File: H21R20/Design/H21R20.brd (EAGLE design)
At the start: 34.6 x 30 mm, 52 parts, among them IC1 ESP32-C3-MINI-1-N4, P1 HEXABIT_17.32_NO_P6_P7_P12, U1 STM32G0B1CEU6NUFQFPN48_STM32_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, X1 8MHZ

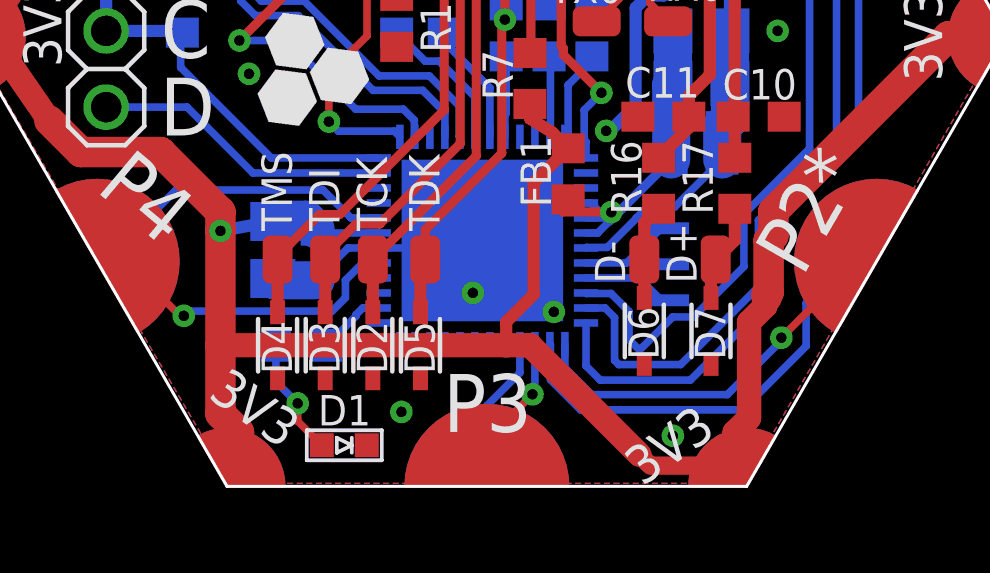
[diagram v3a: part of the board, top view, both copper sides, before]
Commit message: -Correcting some documentaion issues
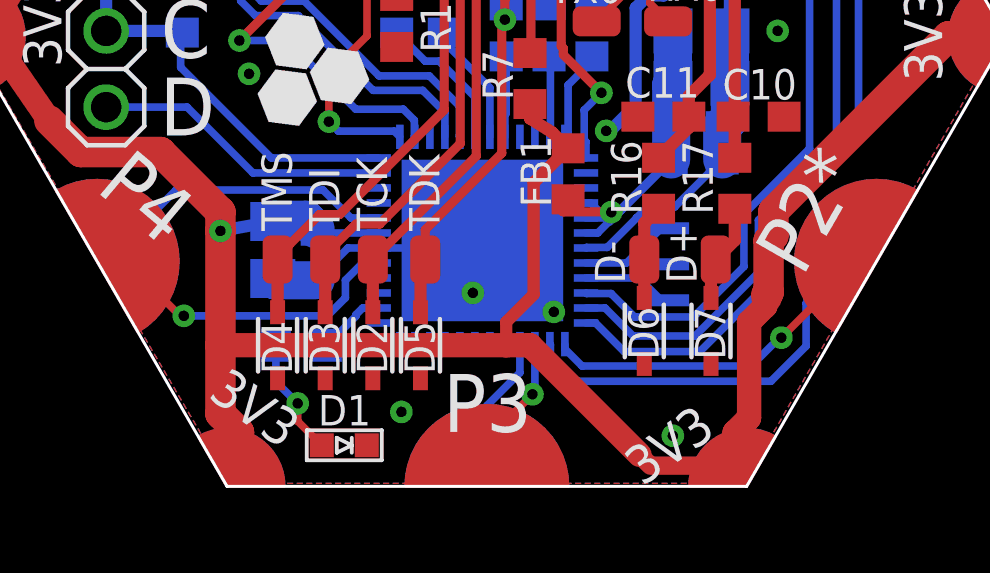
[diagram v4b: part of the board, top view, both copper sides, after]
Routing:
- net USART4_RX: track 26.0 -> 24.0 mm
- net USART4_TX: track 25.3 -> 23.4 mm
- net N$12: track 21.0 -> 19.6 mm
- net USART2_TX: track 13.5 -> 12.3 mm
- net USART2_RX: track 14.9 -> 13.8 mm
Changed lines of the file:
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@@
 <?xml version="1.0" encoding="utf-8"?>
 <!DOCTYPE eagle SYSTEM "eagle.dtd">
-<eagle version="9.6.2">
+<eagle version="9.6.1">
 <drawing>
 <settings>
-<setting alwaysvectorfont="no"/>
+<setting alwaysvectorfont="yes"/>
 <setting verticaltext="up"/>
 </settings>
@@
 </layers>
 <board>
-<fusionsync huburn="a.YnVzaW5lc3M6Z21haWwyMzYzMzA4" projecturn="a.YnVzaW5lc3M6Z21haWwyMzYzMzA4I0QyMDIyMDIyNzUwMTk3Njc4MQ" f3durn="urn:adsk.wipprod:dm.lineage:qXE8OnRfQE6j2yabujY-pQ" pcbguid="" lastpulledtime="" lastsyncedchangeguid="" latestrevisionid="54fbac2f-ec53-449b-82c3-dd918a9148f3" lastsyncedrevisionid="54fbac2f-ec53-449b-82c3-dd918a9148f3" lastboardhashguid="b3c6bdbd-b9b3-ff31-31e0-f0e2b1b9bcbe" lastpushedtime="2022-10-21T21:13:56Z" linktopcb3d="true"/>
+<fusionsync huburn="a.YnVzaW5lc3M6Z21haWwyMzYzMzA4" projecturn="a.YnVzaW5lc3M6Z21haWwyMzYzMzA4I0QyMDIyMDIyNzUwMTk3Njc4MQ" f3durn="urn:adsk.wipprod:dm.lineage:qXE8OnRfQE6j2yabujY-pQ" pcbguid="" lastpulledtime="" lastsyncedchangeguid="" latestrevisionid="54fbac2f-ec53-449b-82c3-dd918a9148f3" lastsyncedrevisionid="54fbac2f-ec53-449b-82c3-dd918a9148f3" lastboardhashguid="b3c6bdbd-b9b3-ff31-31e0-f0e2b1b9bcbe" lastpushedtime="2022-10-21T21:13:56Z" linktopcb3d="%12"/>
 <plain>
 <text x="14.5325" y="15.09375" size="1.27" layer="21" font="vector" rot="R90" align="center">3V3</text>
@@
 <wire x1="11.6462" y1="19.463765625" x2="11.6462" y2="11.53495" width="0.254" layer="16"/>
 <wire x1="11.6462" y1="11.53495" x2="9.0424" y2="8.93115" width="0.254" layer="16"/>
-<wire x1="9.0424" y1="8.93115" x2="9.0424" y2="6.70865" width="0.254" layer="16"/>
-<wire x1="4.38814375" y1="4.11815625" x2="4.24815" y2="4.25815" width="0.254" layer="16"/>
-<wire x1="4.24815" y1="5.6869" x2="3.93065" y2="6.0044" width="0.254" layer="16"/>
+<wire x1="9.0424" y1="8.93115" x2="9.0424" y2="7.1849" width="0.254" layer="16"/>
+<wire x1="4.88315" y1="5.0519" x2="3.93065" y2="6.0044" width="0.254" layer="16"/>
 <wire x1="3.29565" y1="6.0044" x2="3.93065" y2="6.0044" width="0.254" layer="16"/>
-<wire x1="4.24815" y1="5.6869" x2="4.24815" y2="4.25815" width="0.254" layer="16"/>
-<wire x1="6.45190625" y1="4.11815625" x2="4.38814375" y2="4.11815625" width="0.254" layer="16"/>
-<wire x1="9.0424" y1="6.70865" x2="6.45190625" y2="4.11815625" width="0.254" layer="16"/>
+<wire x1="4.88315" y1="5.0519" x2="4.88315" y2="5.07065625" width="0.254" layer="16"/>
+<wire x1="6.92815625" y1="5.07065625" x2="4.88315" y2="5.07065625" width="0.254" layer="16"/>
+<wire x1="9.0424" y1="7.1849" x2="6.92815625" y2="5.07065625" width="0.254" layer="16"/>
 </signal>
 <signal name="USART4_RX">
 <contactref element="U1" pad="12"/>
 <contactref element="P1" pad="PAD_PD1"/>
-<wire x1="3.7719" y1="3.5993" x2="3.29565" y2="4.07555" width="0.254" layer="16"/>
-<wire x1="3.29565" y1="5.5043" x2="3.29565" y2="4.07555" width="0.254" layer="16"/>
-<wire x1="3.7719" y1="3.5993" x2="6.7743" y2="3.5993" width="0.254" layer="16"/>
-<wire x1="6.7743" y1="3.5993" x2="9.525" y2="6.35" width="0.254" layer="16"/>
-<wire x1="9.525" y1="6.35" x2="9.525" y2="8.73125" width="0.254" layer="16"/>
+<wire x1="4.56565" y1="4.5518" x2="3.61315" y2="5.5043" width="0.254" layer="16"/>
+<wire x1="3.29565" y1="5.5043" x2="3.61315" y2="5.5043" width="0.254" layer="16"/>
+<wire x1="4.56565" y1="4.5518" x2="7.0918" y2="4.5518" width="0.254" layer="16"/>
+<wire x1="7.0918" y1="4.5518" x2="9.525" y2="6.985" width="0.254" layer="16"/>
+<wire x1="9.525" y1="6.985" x2="9.525" y2="8.73125" width="0.254" layer="16"/>
 <wire x1="12.38" y1="11.58625" x2="12.38" y2="22.20875" width="0.254" layer="16"/>
 <wire x1="9.525" y1="8.73125" x2="12.38" y2="11.58625" width="0.254" layer="16"/>
@@
 <contactref element="P1" pad="PAD_PU2"/>
 <via x="9.8085125" y="5.015303125" extent="1-16" drill="0.35"/>
-<wire x1="2.59195" y1="4.8006" x2="2.59195" y2="4.00685" width="0.254" layer="16"/>
-<wire x1="3.4821" y1="3.1167" x2="2.59195" y2="4.00685" width="0.254" layer="16"/>
-<wire x1="8.007240625" y1="3.1167" x2="3.4821" y2="3.1167" width="0.254" layer="16"/>
-<wire x1="9.8085125" y1="5.015303125" x2="9.857178125" y2="4.9666375" width="0.254" layer="16"/>
-<wire x1="9.857178125" y1="4.9666375" x2="8.007240625" y2="3.1167" width="0.254" layer="16"/>
+<wire x1="3.1646" y1="4.0692" x2="2.59195" y2="4.64185" width="0.254" layer="16"/>
+<wire x1="2.59195" y1="4.8006" x2="2.59195" y2="4.64185" width="0.254" layer="16"/>
+<wire x1="8.800990625" y1="4.0692" x2="3.1646" y2="4.0692" width="0.254" layer="16"/>
+<wire x1="9.8085125" y1="5.015303125" x2="9.74709375" y2="5.015303125" width="0.254" layer="16"/>
+<wire x1="9.74709375" y1="5.015303125" x2="8.800990625" y2="4.0692" width="0.254" layer="16"/>
 <wire x1="11.860071875" y1="6.785746875" x2="10.732403125" y2="6.227990625" width="0.254" layer="1"/>
 <wire x1="10.8962375" y1="6.103028125" x2="9.8085125" y2="5.015303125" width="0.254" layer="1"/>
@@
 <contactref element="U1" pad="14"/>
 <contactref element="P1" pad="PAD_PD2"/>
-<wire x1="2.10935" y1="3.61190625" x2="3.11140625" y2="2.60985" width="0.254" layer="16"/>
+<wire x1="2.10935" y1="4.24690625" x2="2.79390625" y2="3.56235" width="0.254" layer="16"/>
 <wire x1="10.63375" y1="6.1625" x2="10.63375" y2="4.73375" width="0.254" layer="16"/>
 <wire x1="10.63375" y1="6.1625" x2="12.38" y2="7.90875" width="0.254" layer="16"/>
-<wire x1="10.63375" y1="4.73375" x2="8.50985" y2="2.60985" width="0.254" layer="16"/>
+<wire x1="10.63375" y1="4.73375" x2="9.46235" y2="3.56235" width="0.254" layer="16"/>
 <wire x1="2.09185" y1="4.8006" x2="2.10935" y2="4.7831" width="0.254" layer="16"/>
-<wire x1="2.10935" y1="4.7831" x2="2.10935" y2="3.61190625" width="0.254" layer="16"/>
-<wire x1="3.11140625" y1="2.60985" x2="8.50985" y2="2.60985" width="0.254" layer="16"/>
+<wire x1="2.10935" y1="4.7831" x2="2.10935" y2="4.24690625" width="0.254" layer="16"/>
+<wire x1="2.79390625" y1="3.56235" x2="9.46235" y2="3.56235" width="0.254" layer="16"/>
 </signal>
 <signal name="USART1_TX">
@@
 <via x="-10.11095625" y="5.74235" extent="1-16" drill="0.35"/>
 <wire x1="-4.14934375" y1="7.5048" x2="-4.7244" y2="6.92974375" width="0.254" layer="16"/>
-<wire x1="-5.165415625" y1="5.9011" x2="-9.95220625" y2="5.9011" width="0.254" layer="16"/>
-<wire x1="-9.95220625" y1="5.9011" x2="-10.11095625" y2="5.74235" width="0.254" layer="16"/>
+<wire x1="-5.324165625" y1="5.74235" x2="-10.11095625" y2="5.74235" width="0.254" layer="16"/>
 <wire x1="-4.7244" y1="6.92974375" x2="-4.7244" y2="6.342115625" width="0.254" layer="16"/>
-<wire x1="-4.7244" y1="6.342115625" x2="-5.165415625" y2="5.9011" width="0.254" layer="16"/>
+<wire x1="-4.7244" y1="6.342115625" x2="-5.324165625" y2="5.74235" width="0.254" layer="16"/>
 <wire x1="-10.11095625" y1="5.74235" x2="-10.2336" y2="5.74235" width="0.254" layer="1"/>
 <wire x1="-10.2336" y1="5.74235" x2="-12.4" y2="7.90875" width="0.254" layer="1"/>
@@
 <wire x1="3.29565" y1="6.5046" x2="3.31325" y2="6.487" width="0.254" layer="16"/>
 <wire x1="3.31325" y1="6.487" x2="4.13055" y2="6.487" width="0.254" layer="16"/>
-<wire x1="4.13055" y1="6.487" x2="4.73075" y2="5.8868" width="0.254" layer="16"/>
-<wire x1="4.73075" y1="4.95000625" x2="5.08" y2="4.60075625" width="0.254" layer="16"/>
-<wire x1="5.08" y1="4.60075625" x2="6.1849" y2="5.70565625" width="0.254" layer="16"/>
-<wire x1="6.1849" y1="5.70565625" x2="6.87979375" y2="5.70565625" width="0.254" layer="16"/>
+<wire x1="4.13055" y1="6.487" x2="4.92386875" y2="5.69368125" width="0.254" layer="16"/>
+<wire x1="4.92386875" y1="5.69368125" x2="4.93584375" y2="5.70565625" width="0.254" layer="16"/>
+<wire x1="4.93584375" y1="5.70565625" x2="6.87979375" y2="5.70565625" width="0.254" layer="16"/>
 <wire x1="10.7475" y1="11.31875" x2="8.5598" y2="9.13105" width="0.254" layer="16"/>
 <wire x1="6.87979375" y1="5.70565625" x2="8.5598" y2="7.3856625" width="0.254" layer="16"/>
 <wire x1="8.5598" y1="7.3856625" x2="8.5598" y2="9.13105" width="0.254" layer="16"/>
-<wire x1="4.73075" y1="5.8868" x2="4.73075" y2="4.95000625" width="0.254" layer="16"/>
 <wire x1="10.31875" y1="17.78" x2="10.7475" y2="17.35125" width="0.254" layer="16"/>
 <wire x1="10.7475" y1="17.35125" x2="10.7475" y2="11.31875" width="0.254" layer="16"/>
@@
 <mfgpreviewcolor name="substratecolor" color="0xFF786E46"/>
 </mfgpreviewcolors>
-<errors>
-</errors>
 </board>
 </drawing>

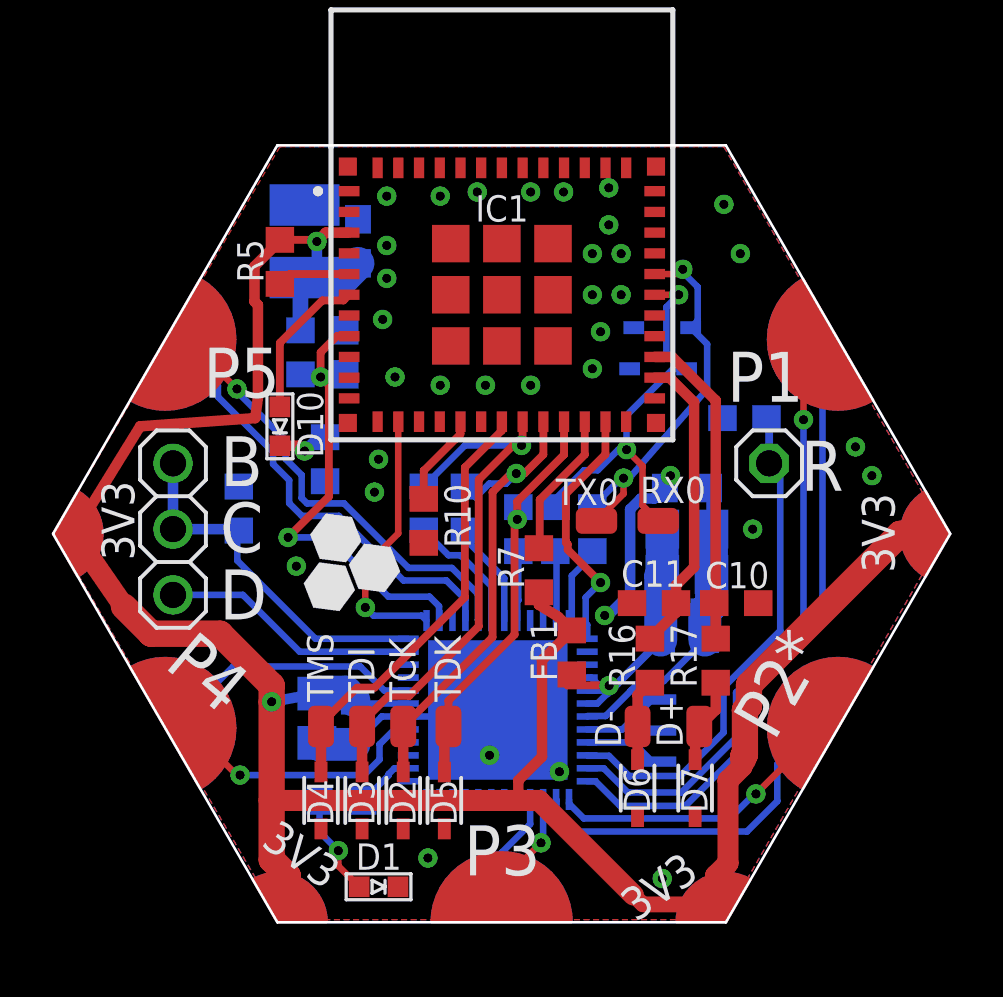
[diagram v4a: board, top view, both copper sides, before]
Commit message: -Improve the layout design -Change the jumber resistors footprint to 0402
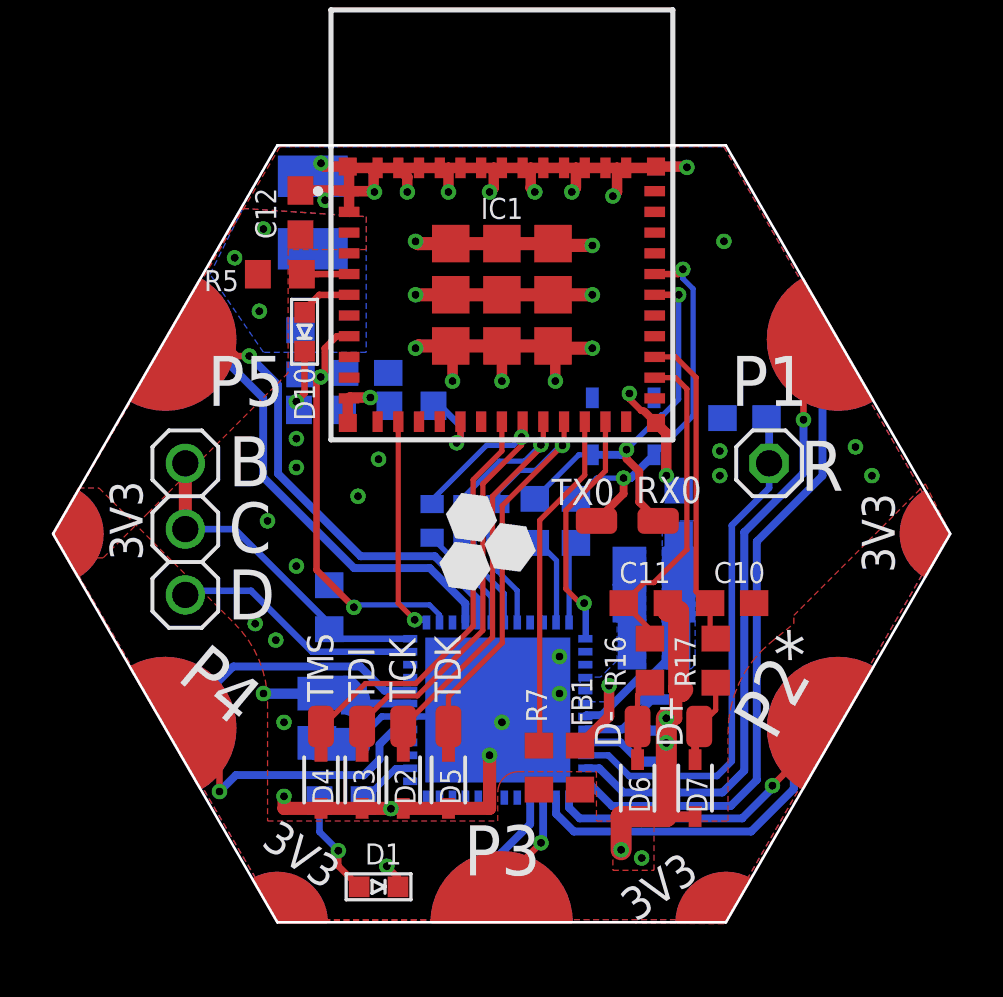
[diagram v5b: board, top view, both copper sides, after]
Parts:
- R11, R12, R13: device HEXABITZ_RCLS:R-0603 -> HEXABITZ_RCLS:R-0402
- U1: value STM32G0B1CEU6NUFQFPN48_STM32_STM -> STM32G0B1CEU6N; device HEXABITZ_ICs:UFQFPN48_STM32_STM -> HEXABITZ_ICs:HEXABITZ_ICS_QFN_B1CEU6_STM-L
- moved R7 7.62 mm to (1.43, 6.03)
- moved R2 5.17 mm to (-6.67, 12.2)
- moved R10 4.47 mm to (-3.49, 20.0), flipped to the bottom, turned to 0 degrees
- moved FB1 4.46 mm to (3.02, 6.03), turned to 90 degrees
- moved D8 3.82 mm to (5.87, 19.2), turned to 270 degrees
- moved D10 3.77 mm to (-7.62, 22.9)
- moved D9 3.38 mm to (3.49, 19.2), turned to 270 degrees
- moved C12 2.48 mm to (-7.78, 27.5), flipped to the top
- moved R4 1.91 mm to (-6.99, 19.8), turned to 0 degrees
- moved C6 1.91 mm to (5.87, 13.8)
- moved C3 1.69 mm to (5.87, 12.4)
- moved C5 1.37 mm to (5.87, 11.3)
- moved C1 1.28 mm to (5.87, 10.3)
- moved C13 1.16 mm to (-7.30, 27.5)
- moved C2 1.12 mm to (-5.24, 21.3), turned to 0 degrees
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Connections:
- net GND: no longer U1.2, U1.3
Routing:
- net VDD: track 97.4 -> 5.88 mm, vias 2 -> 4
- net GND: track 13.8 -> 89.9 mm, vias 34 -> 47
- net VDDA: track 13.0 -> 2.78 mm
- net N$4: track 5.62 -> 13.2 mm
- net VSSA: track 11.8 -> 4.46 mm
- net N$14: track 5.91 -> 2.06 mm
- net N$11: track 15.9 -> 18.3 mm
- net ESP32_CS: track 10.3 -> 8.48 mm
- net USART1_TX: track 10.8 -> 12.1 mm
- net ESP32_RESET: track 18.7 -> 17.5 mm
- net USART4_RX: track 24.0 -> 25.1 mm
- net C: track 14.2 -> 13.1 mm
- net N$15: track 2.83 -> 1.82 mm
- net USART4_TX: track 23.4 -> 24.4 mm
- net DATA_N: track 11.8 -> 12.7 mm
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- added copper zone on layer 1, net VDD
- added copper zone on layer 16, net VDD
- added copper zone on layer 16, net VDDA
- added copper zone on layer 16, net VSSA
